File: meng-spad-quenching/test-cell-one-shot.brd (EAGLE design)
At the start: 50.8 x 50.8 mm, 41 parts, among them IC1 NC7SV74K8X, IC2 LTC1711, IC3 DS1100LU-20+, M1 BSS806N, X1 CONN_3V3_PWR, X2 CONN_ONE_SHOT_OUT, X3 CONN_TRIG_IN, X4 CONN_ONE_SHOT_OUT_DLY

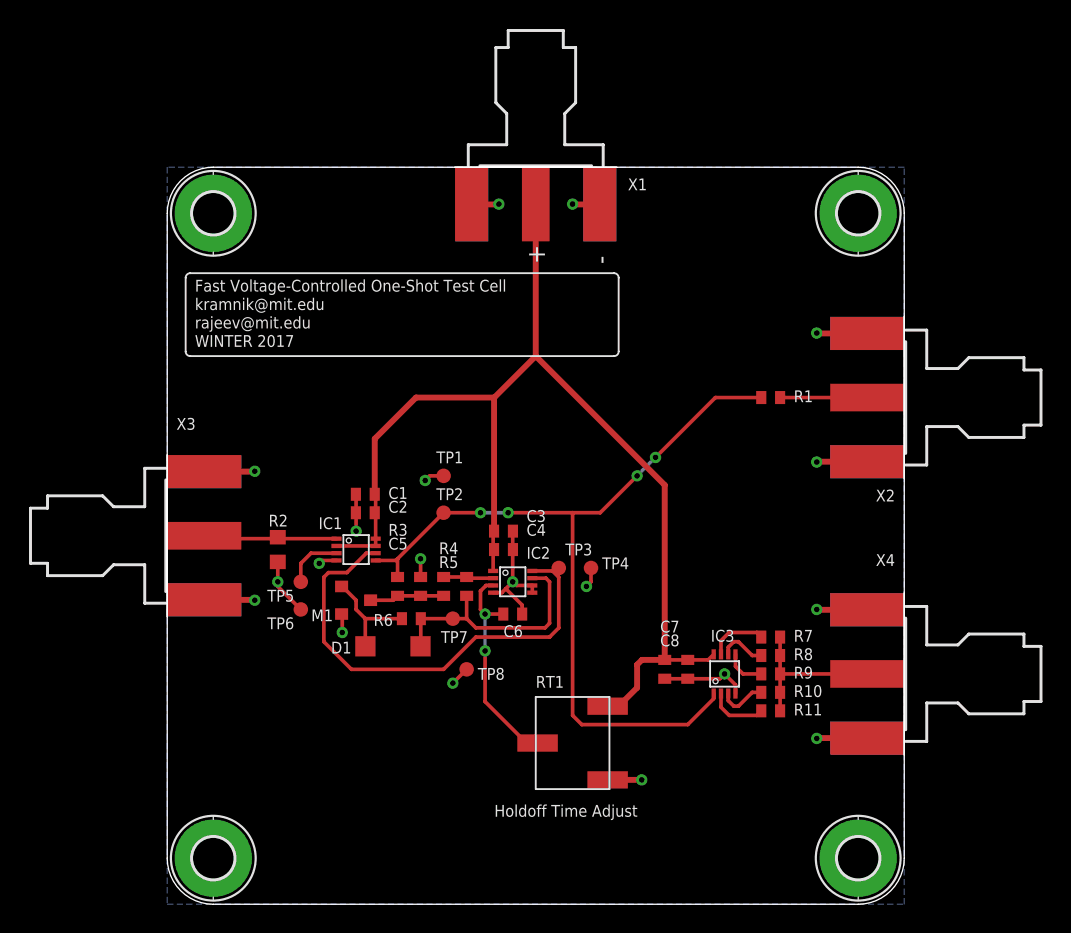
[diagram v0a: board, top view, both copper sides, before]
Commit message: Added EXT vref conn, finalized gerbers
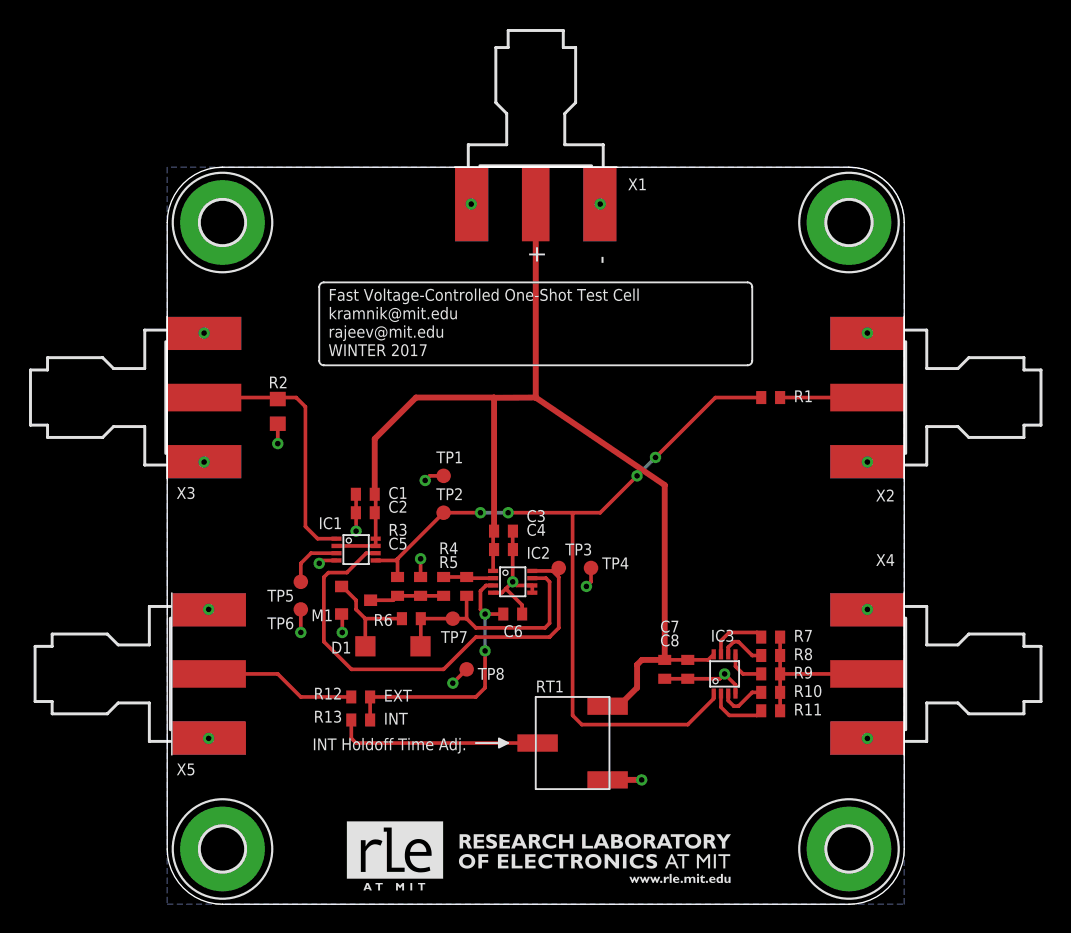
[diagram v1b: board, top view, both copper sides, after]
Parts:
- added R12, R13: DNP, rcl:R0402
- added X5: CONN_VREF_EXT, con-coax:J502-ND-142-0711-871/876
- H1, H2, H3, H4: value MOUNT-PAD-ROUND2.8 -> MOUNT-PAD-ROUND3.0; device holes:2,8-PAD -> holes:3,0-PAD
- moved X3 9.52 mm to (0.00, 34.9)
- moved R2 9.52 mm to (7.62, 34.0)
- moved H3 0.90 mm to (3.81, 3.81)
- moved H1 0.90 mm to (3.81, 47.0)
- moved H4 0.90 mm to (47.0, 3.81)
- moved H2 0.90 mm to (47.0, 47.0)
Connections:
- new net COMP_VREF_EXT: R12.1, X5.1
- new net COMP_VREF_INT: R13.1, RT1.2
- net GND: now also H1.B3,0, H2.B3,0, H3.B3,0, H4.B3,0, X5.G@1, X5.G@2, X5.G@3, X5.G@4; no longer H1.B2,8, H2.B2,8, H3.B2,8, H4.B2,8
- net ONE_SHOT_VREF: now also R12.2, R13.2; no longer RT1.2
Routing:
- net GND: track 57.3 -> 32.6 mm, vias 19 -> 22
- net COMP_VREF_INT: track 0.00 -> 14.2 mm
- net COMP_VREF_EXT: track 0.00 -> 10.5 mm
- net HOLDOFF_TRIG: track 9.29 -> 18.1 mm
- net ONE_SHOT_VREF: track 14.8 -> 18.9 mm
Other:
- outline, holes or cut-outs redrawn
- board text added: "EXT"
- board text added: "INT"
- board text added: "INT Holdoff Time Adj."
- board text removed: "Holdoff Time Adjust"
